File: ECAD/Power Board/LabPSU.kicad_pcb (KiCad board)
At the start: 2 copper layers, 92 parts, among them J1 PWR, J2 CTRL, J3 UPDI, J4 +, J5 -, Q1 Si7148DP, Q2 Si7148DP, U1 LM317_TO-220, U10 LM358, U11 ATtiny414-SS, U12 MCP4811, U13 INA180A3, U2 LM1117-3.3, U3 MCP4811, U4 INA180A3, U5 LM358, U6 TXB0104D, U8 LM5118MH

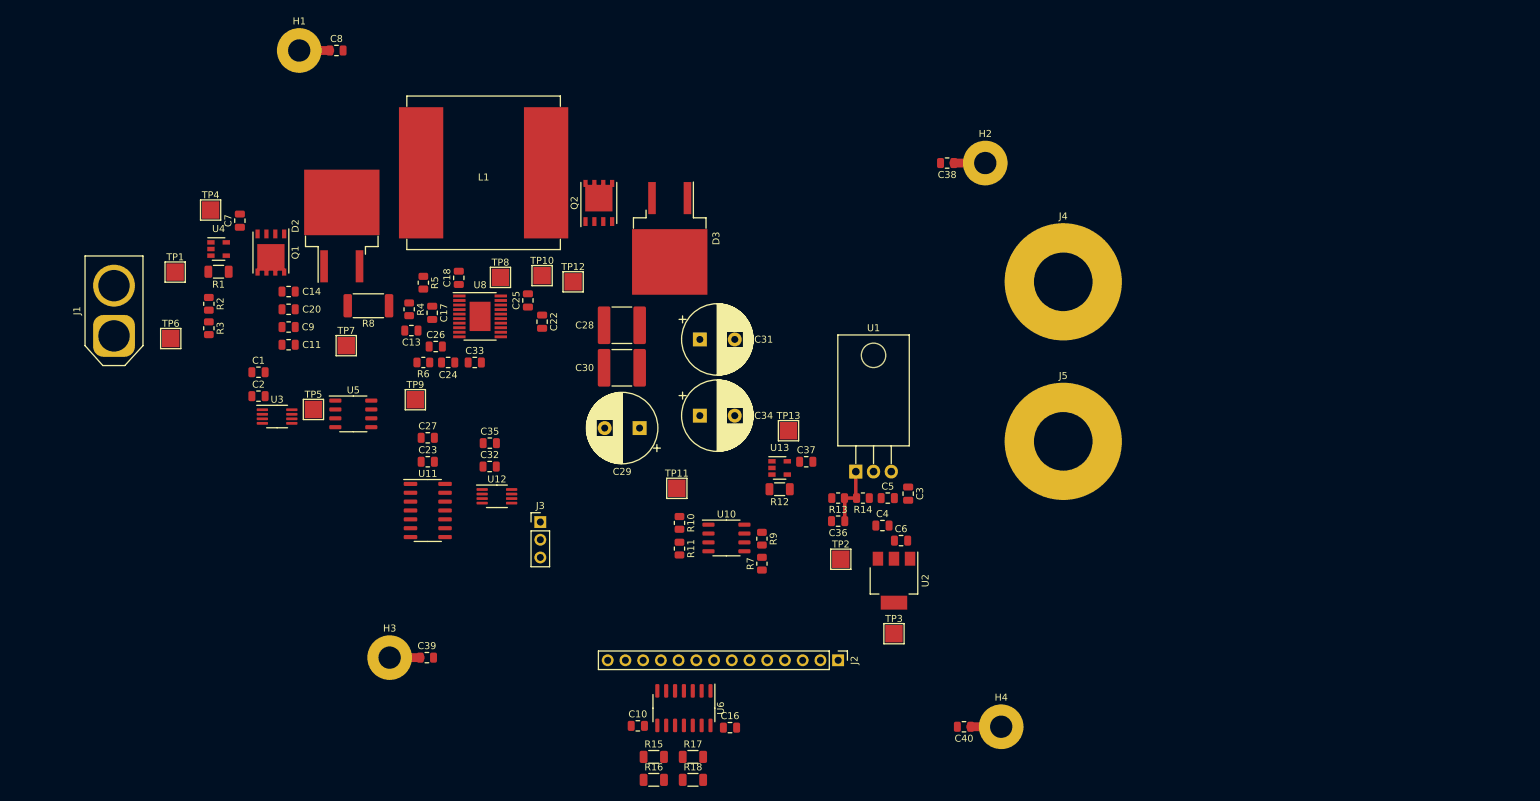
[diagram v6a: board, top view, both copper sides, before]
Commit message: cleanup main schematic, remove mppt circuitry
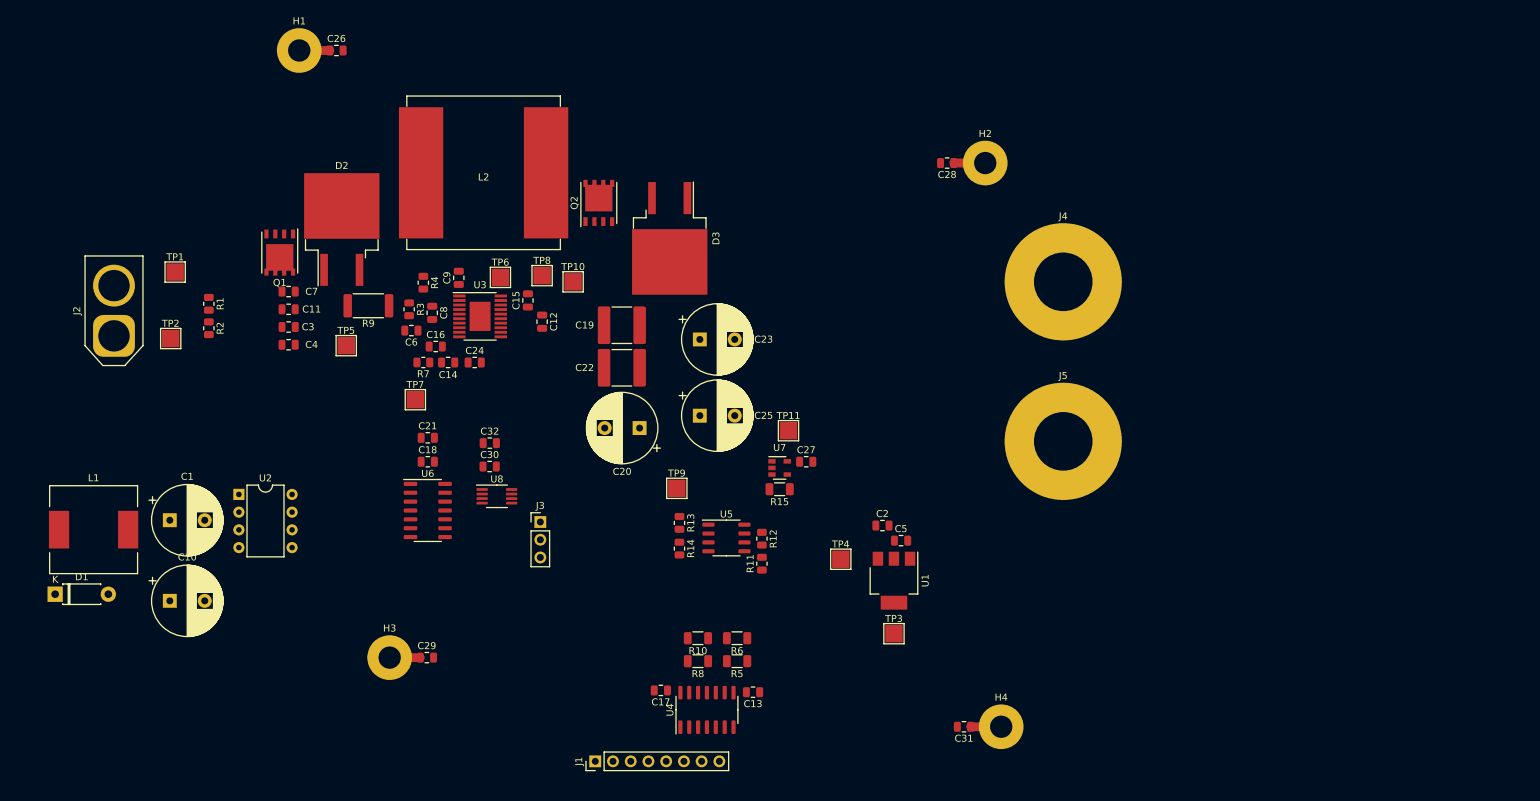
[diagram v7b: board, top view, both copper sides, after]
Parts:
- removed the C2 at (65.5, 104.4)
- removed the C3 at (158.6, 118.4)
- removed C36: 1uF, Capacitor_SMD:C_0805_2012Metric
- removed the C5 at (155.7, 119.0)
- removed the C7 at (62.9, 79.2)
- removed the J2 at (148.6, 142.2)
- removed the R1 at (59.8, 86.6)
- removed the R13 at (148.6, 119.0)
- removed the R14 at (152.1, 119.0)
- removed the TP4 at (58.7, 77.7)
- removed the TP5 at (73.4, 106.3)
- removed the U1 at (151.1, 115.2)
- removed the U3 at (68.2, 107.3)
- removed the U4 at (59.8, 83.3)
- removed the U5 at (79.1, 106.9)
- added C10: 220uF, Capacitor_THT:CP_Radial_D10.0mm_P5.00mm, F.Cu at (52.8, 133.7)
- added D1: SB190-T, Diode_THT:D_DO-41_SOD81_P7.62mm_Horizontal, F.Cu at (36.4, 132.8)
- added J1: CTRL, Connector_PinHeader_2.54mm:PinHeader_1x08_P2.54mm_Vertical, F.Cu at (113.8, 156.7)
- added L1: 470uH, Inductor_SMD:L_12x12mm_H8mm, F.Cu at (41.9, 123.5)
- added U2: LM2594HVN-5.0, Package_DIP:DIP-8_W7.62mm, F.Cu at (62.7, 118.5)
- C1: value 10uF -> 220uF; footprint Capacitor_SMD:C_0805_2012Metric -> Capacitor_THT:CP_Radial_D10.0mm_P5.00mm
- J2: renamed from J1; value PWR -> DC-IN
- R1: renamed from R2; value 150K -> 90K
- moved C1 24.7 mm to (52.8, 122.2)
- moved R6 23.5 mm to (134.1, 139.1), turned to 180 degrees
- moved R10 20.3 mm to (128.5, 139.1), turned to 180 degrees
- moved R5 18.2 mm to (134.1, 142.4), turned to 180 degrees
- moved C13 17.2 mm to (136.4, 146.8), turned to 180 degrees
- moved R8 13.7 mm to (128.5, 142.4), turned to 180 degrees
- moved C17 11.3 mm to (123.2, 146.6), turned to 180 degrees
- moved U4 3.31 mm to (129.8, 149.4), turned to 90 degrees
- moved Q1 1.27 mm to (68.6, 83.8)
- moved D2 0.51 mm to (77.5, 80.5)
- renumbered C20 to C11, C22 to C12, C10 to C13, C24 to C14, C25 to C15, C26 to C16, C16 to C17, C23 to C18, C28 to C19, C4 to C2, C29 to C20, C27 to C21, C30 to C22, C31 to C23, C33 to C24, C34 to C25, C8 to C26, C37 to C27, C38 to C28, C39 to C29, C9 to C3, C32 to C30, C40 to C31, C35 to C32, C11 to C4, C6 to C5, C13 to C6, C14 to C7, C17 to C8, C18 to C9, L1 to L2, R18 to R10, R7 to R11, R9 to R12, R10 to R13, R11 to R14, R12 to R15, R3 to R2, R4 to R3, R5 to R4, R15 to R5, R16 to R6, R6 to R7, R17 to R8, R8 to R9, TP12 to TP10, TP13 to TP11, TP6 to TP2, TP2 to TP4, TP7 to TP5, TP8 to TP6, TP9 to TP7, TP10 to TP8, TP11 to TP9, U2 to U1, U8 to U3, U6 to U4, U10 to U5, U11 to U6, U13 to U7, U12 to U8
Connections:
- C1 pad 1: +3V3 -> VBUS
- C11 pad 1: Net-(C11-Pad1) -> VBUS
- C3 pad 1: Net-(C11-Pad1) -> VBUS
- C4 pad 1: Net-(C11-Pad1) -> VBUS
- C7 pad 1: Net-(C11-Pad1) -> VBUS
- C9 pad 1: Net-(C11-Pad1) -> VBUS
- Q1 pad 5: Net-(C11-Pad1) -> VBUS
- R1 pad 2: Net-(R2-Pad2) -> Net-(R1-Pad2)
- R2 pad 1: Net-(R2-Pad2) -> Net-(R1-Pad2)
- R4 pad 1: Net-(C11-Pad1) -> VBUS
- U3 pad 1: Net-(C11-Pad1) -> VBUS
- U3 pad 2: Net-(U5-Pad1) -> Net-(R1-Pad2)
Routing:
- net Net-(C36-Pad1): track 8.89 -> 0.00 mm

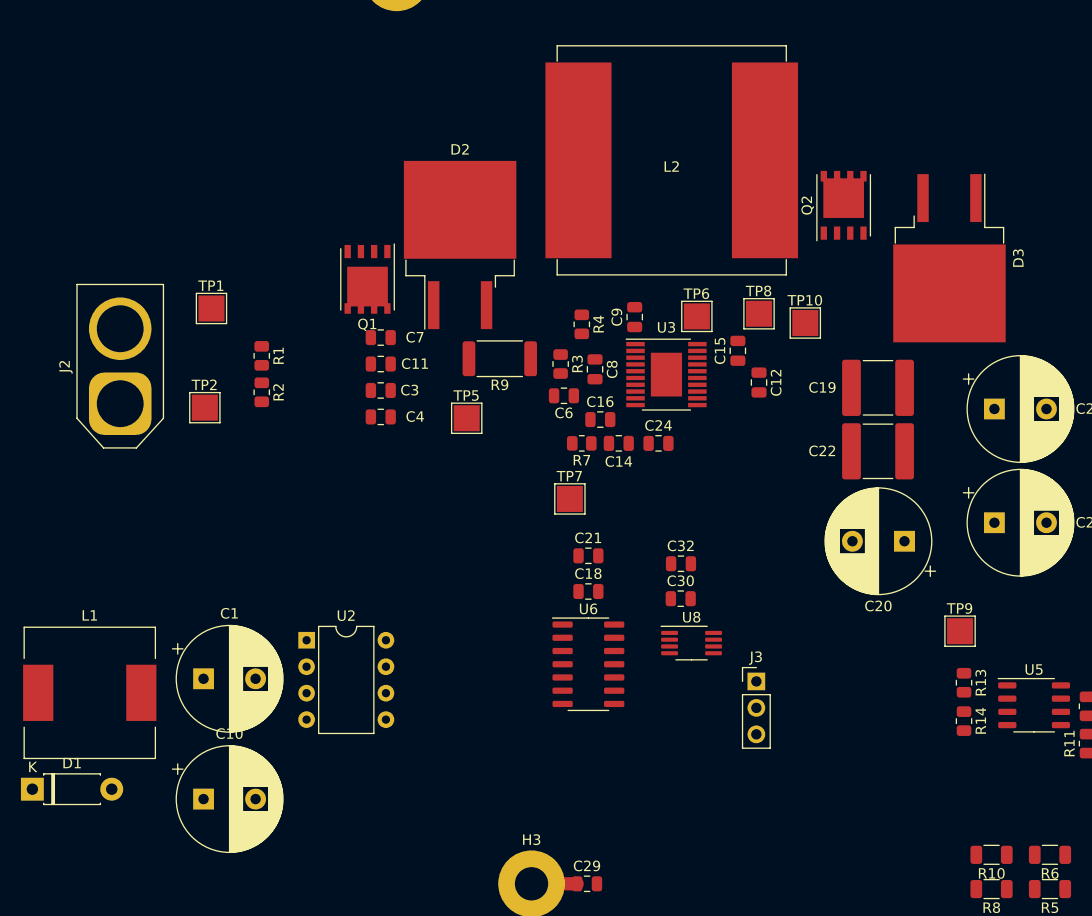
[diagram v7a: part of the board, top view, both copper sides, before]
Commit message: route out larger planes
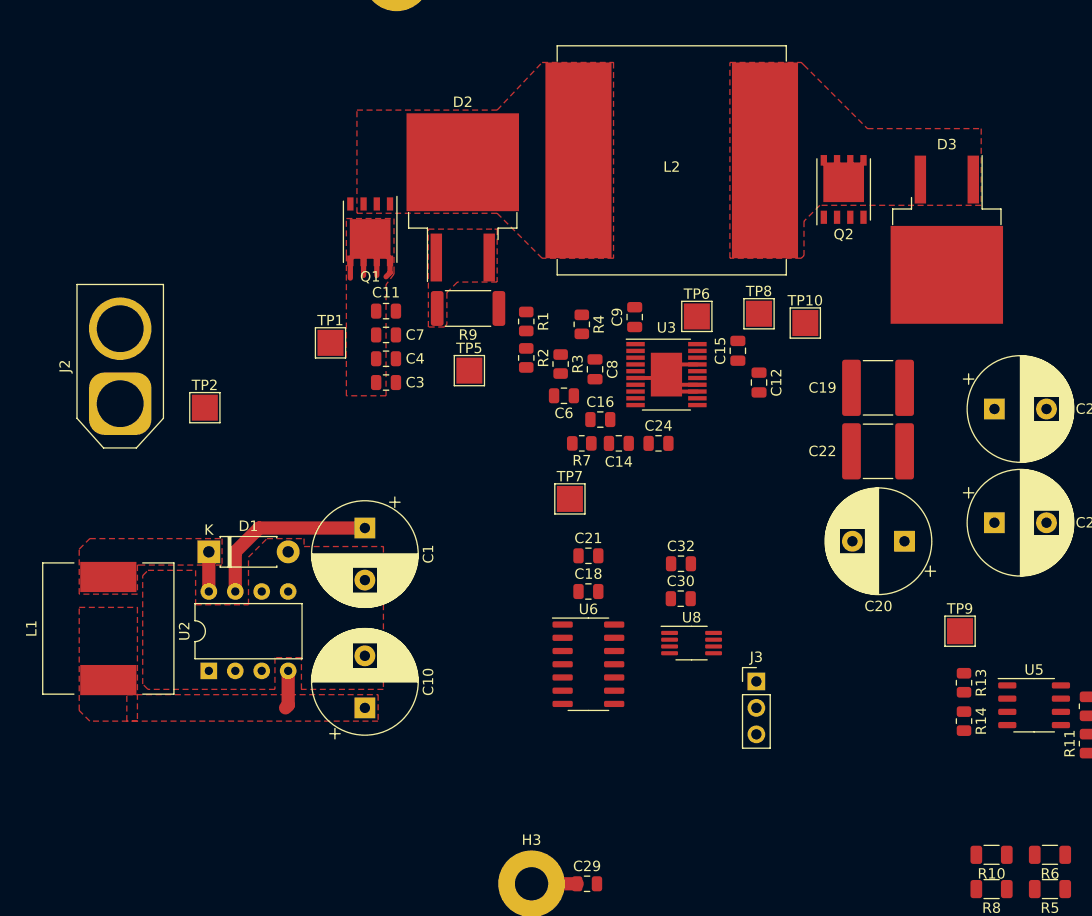
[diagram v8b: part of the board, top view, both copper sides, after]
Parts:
- moved D1 28.4 mm to (53.3, 110.0)
- moved R2 25.6 mm to (83.8, 91.4)
- moved R1 25.6 mm to (83.8, 87.9)
- moved C1 21.2 mm to (68.3, 107.7), turned to 270 degrees
- moved C10 17.8 mm to (68.3, 125.0), turned to 90 degrees
- moved TP1 11.9 mm to (65.0, 89.9)
- moved U2 9.84 mm to (53.3, 121.4), turned to 90 degrees
- moved L1 6.43 mm to (43.7, 117.3), turned to 270 degrees
- moved R9 5.71 mm to (78.2, 86.6)
- moved C4 5.61 mm to (70.4, 91.4)
- moved C11 5.11 mm to (70.4, 86.9)
- moved D2 4.58 mm to (77.7, 75.9)
- moved TP5 4.58 mm to (78.4, 92.6)
- moved Q1 4.58 mm to (68.8, 79.2)
- moved D3 1.80 mm to (124.2, 80.0)
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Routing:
- net VBUS: track 0.00 -> 33.8 mm
- net GND: track 0.00 -> 14.1 mm
- net Net-(D1-Pad1): track 0.00 -> 3.81 mm
- net +5V: track 0.00 -> 3.66 mm
- added copper zone on F.Cu, net +5V
- added copper zone on F.Cu, net GND
- added copper zone on F.Cu, net Net-(C15-Pad2)
- added copper zone on F.Cu, net Net-(D1-Pad1)
- added copper zone on F.Cu, net Net-(D2-Pad2)
- added copper zone on F.Cu, net Net-(D3-Pad2)
- added copper zone on F.Cu, net VBUS
